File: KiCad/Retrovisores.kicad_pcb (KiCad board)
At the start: 2 copper layers, 63 parts, among them J1 Conn_01x02_Pin, J2 DE9_Pins, J4 DE9_Pins, J5 Conn_01x02_Pin, J6 Conn_01x02_Pin, J7 Conn_01x02_Pin, J8 Conn_PIC_ICSP_ICD, Q14 AO3400A, Q15 AO3401A, Q16 AO3400A, Q17 AO3401A, Q18 AO3400A, Q19 AO3401A, Q20 AO3400A, Q21 AO3401A, Q22 AO3400A, Q23 AO3401A, Q24 AO3400A, Q25 AO3401A, Q27 AO3400A, SW1 SW_Push, SW2 SW_Push, SW3 SW_Push, SW4 SW_Push, SW6 SW_Nidec_CAS-120A1, U1 SHTC3, U2 SN65HVD232, U4 LT1117-3.3, U5 TSR3-2450N, U6 VL53L1CXV0FY1, U7 PIC32MX250F128D-IPT, Y1 Crystal

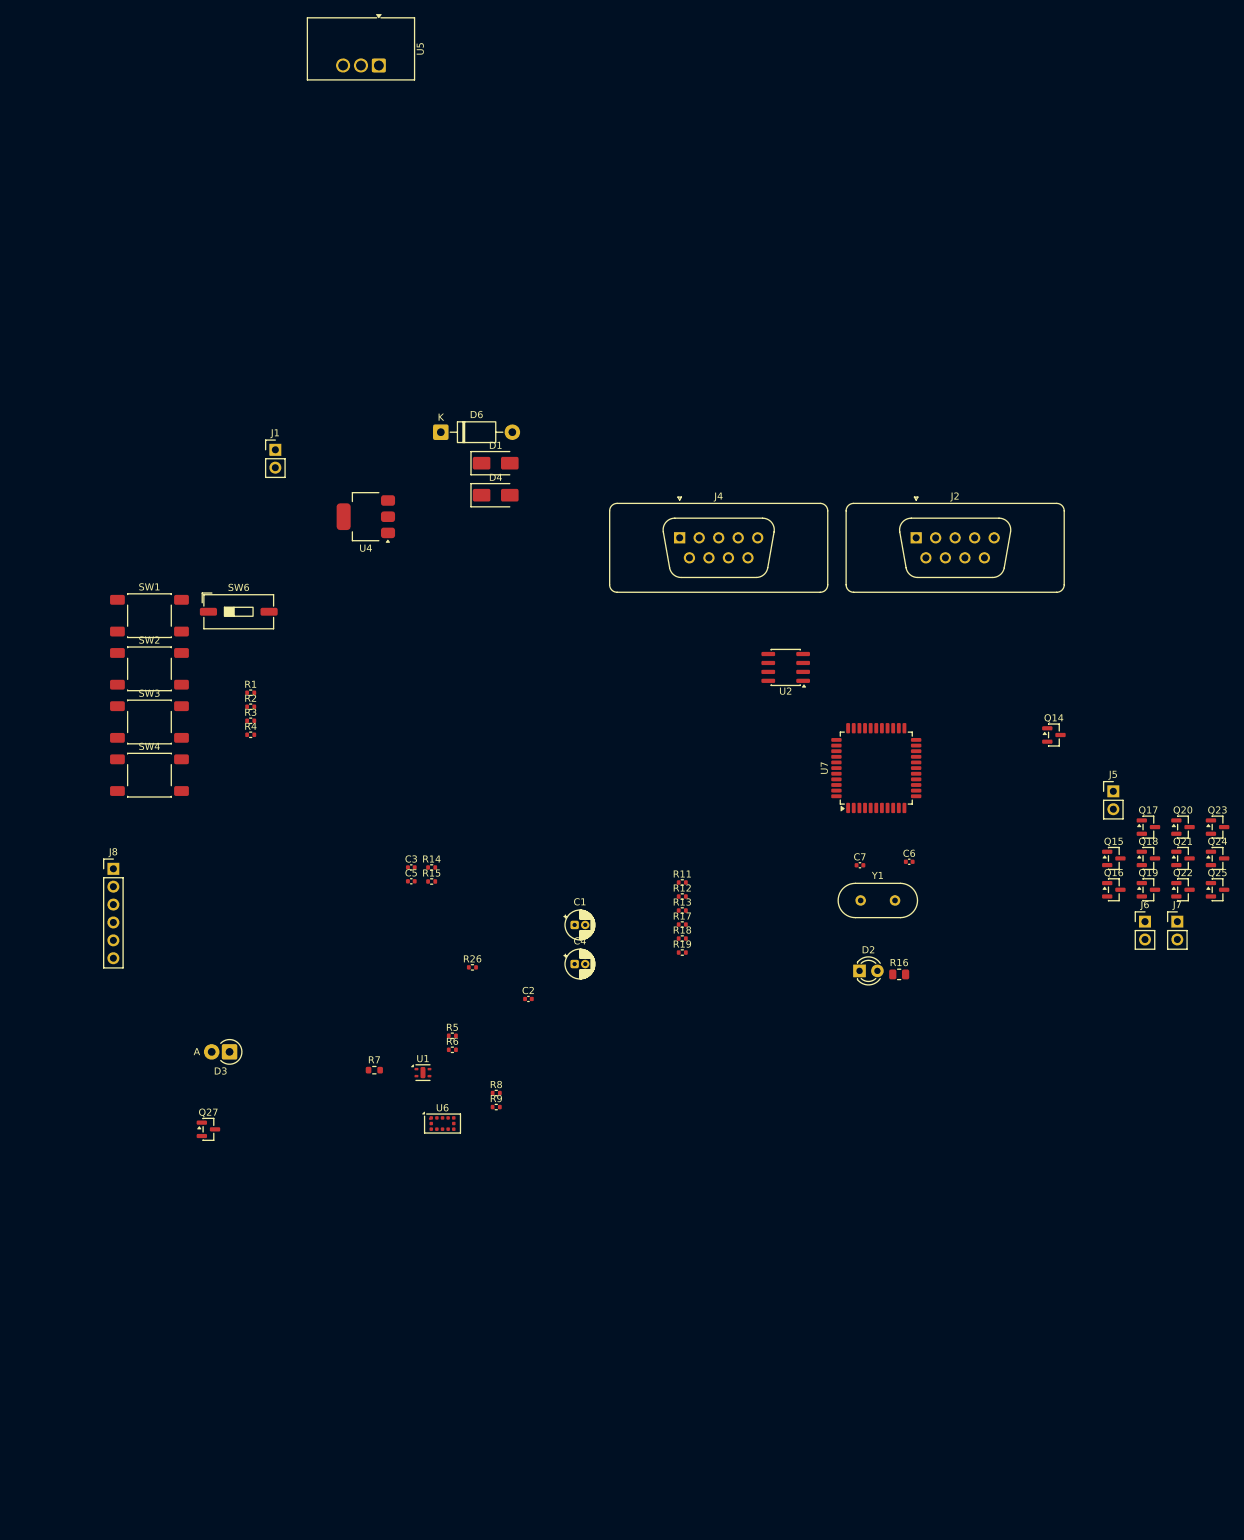
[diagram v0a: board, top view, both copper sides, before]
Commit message: he hecho el layout general menos el calefactor
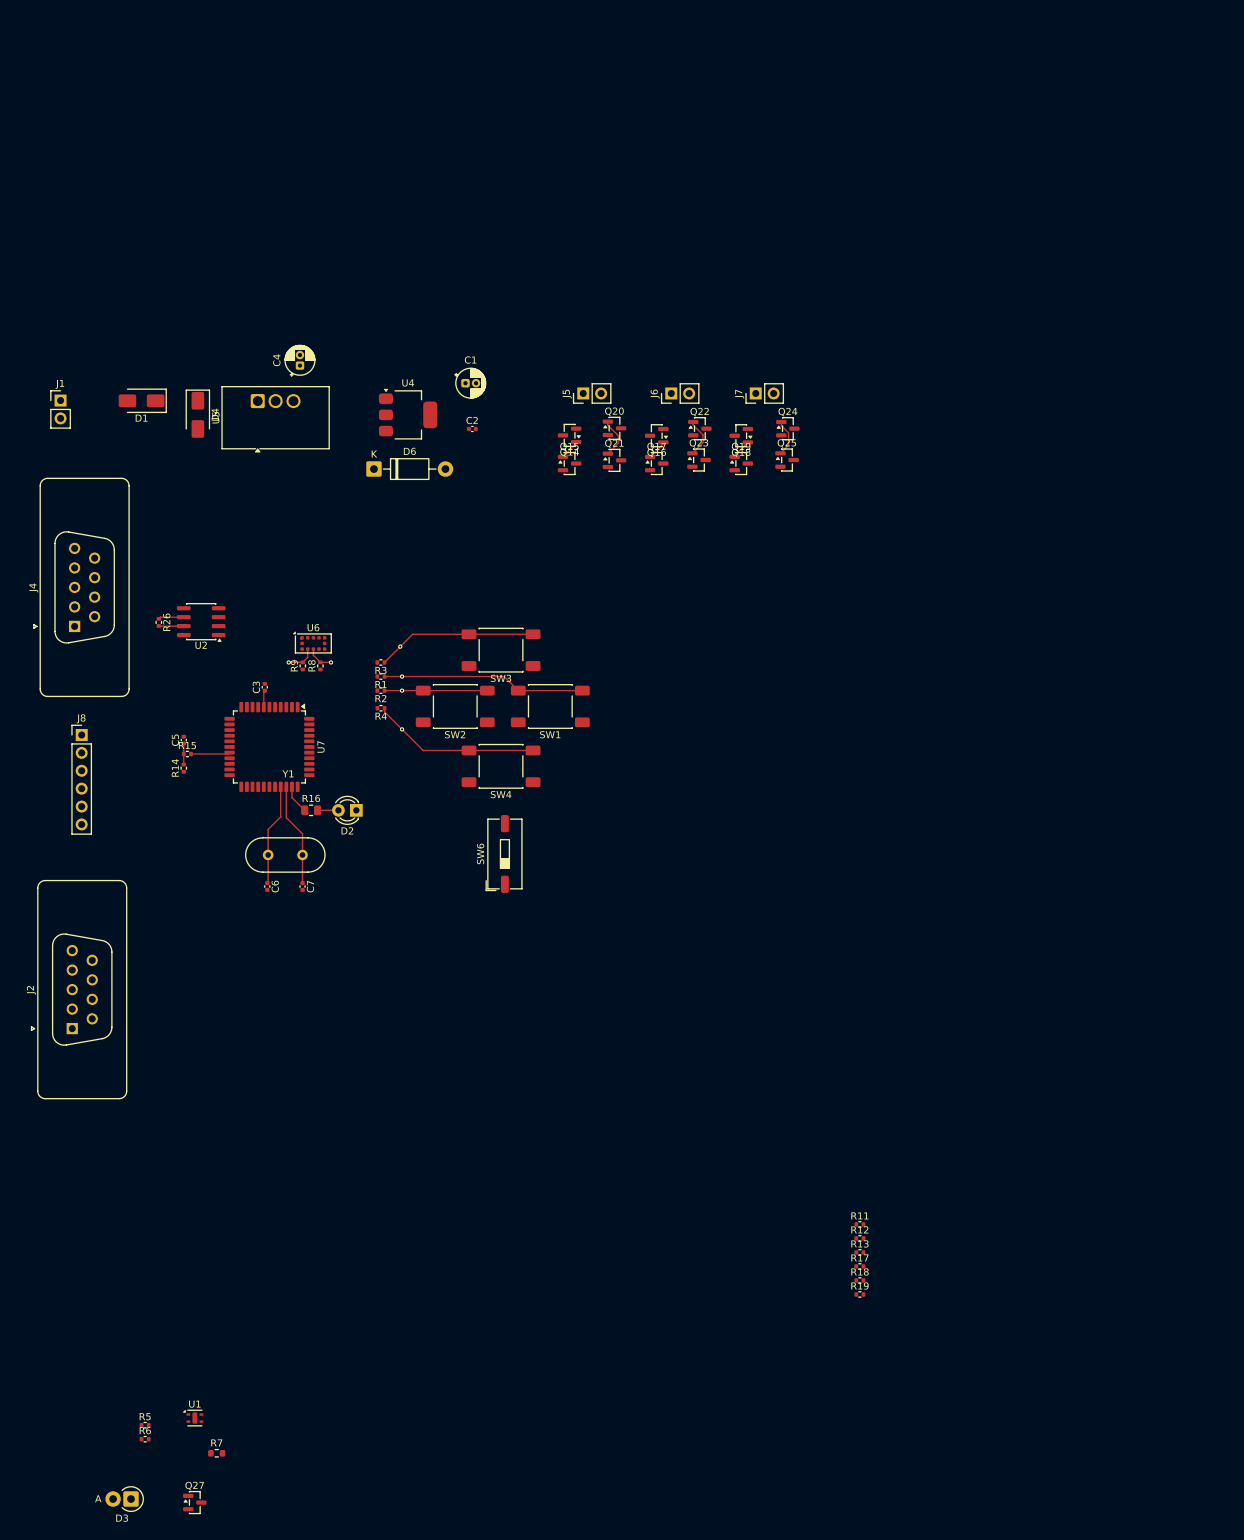
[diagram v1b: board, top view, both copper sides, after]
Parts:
- moved J2 138.6 mm to (93.2, 113.2), turned to 90 degrees
- moved J6 100.8 mm to (178.2, 23.0), turned to 90 degrees
- moved Q20 98.6 mm to (170.2, 27.9)
- moved Q21 98.6 mm to (170.2, 32.5)
- moved J7 96.0 mm to (190.2, 23.0), turned to 90 degrees
- moved Q15 95.5 mm to (163.8, 33.0)
- moved Q22 94.8 mm to (182.3, 28.0)
- moved J5 94.1 mm to (165.7, 23.0), turned to 90 degrees
- moved C4 93.5 mm to (125.5, 19.0), turned to 90 degrees
- moved Q16 91.5 mm to (176.2, 29.0), turned to 180 degrees
- moved C6 91.2 mm to (120.9, 93.0), turned to -90 degrees
- moved Q23 90.2 mm to (182.2, 32.5)
- moved J4 86.8 mm to (93.5, 56.1), turned to 90 degrees
- moved Q17 86.8 mm to (176.2, 33.0)
- moved R16 86.7 mm to (127.1, 82.2)
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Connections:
- U2 pad 1: R -> RCAN
- U2 pad 4: D -> DCAN
- U7 pad 33: R -> RCAN
- U7 pad 41: D -> DCAN
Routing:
- net R: track 0.00 -> 29.6 mm, vias 0 -> 1
- net D: track 0.00 -> 23.9 mm, vias 0 -> 1
- net U: track 0.00 -> 23.1 mm, vias 0 -> 1
- net OSC2: track 0.00 -> 14.6 mm
- net L: track 0.00 -> 14.6 mm, vias 0 -> 1
- net OSC1: track 0.00 -> 14.5 mm
- net SDL1: track 0.00 -> 5.79 mm
- net SDD1: track 0.00 -> 5.64 mm
- net MCLR: track 0.00 -> 5.56 mm
- net CL: track 0.00 -> 5.36 mm
- net KLKI2C: track 0.00 -> 4.18 mm, vias 0 -> 1
- net Net-(U7-RA8): track 0.00 -> 4.09 mm
- net DI2C: track 0.00 -> 3.80 mm, vias 0 -> 1
- net Net-(U2-CANL): track 0.00 -> 3.65 mm
- net Net-(U2-CANH): track 0.00 -> 3.56 mm
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
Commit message: añadido calefactor a la pcb
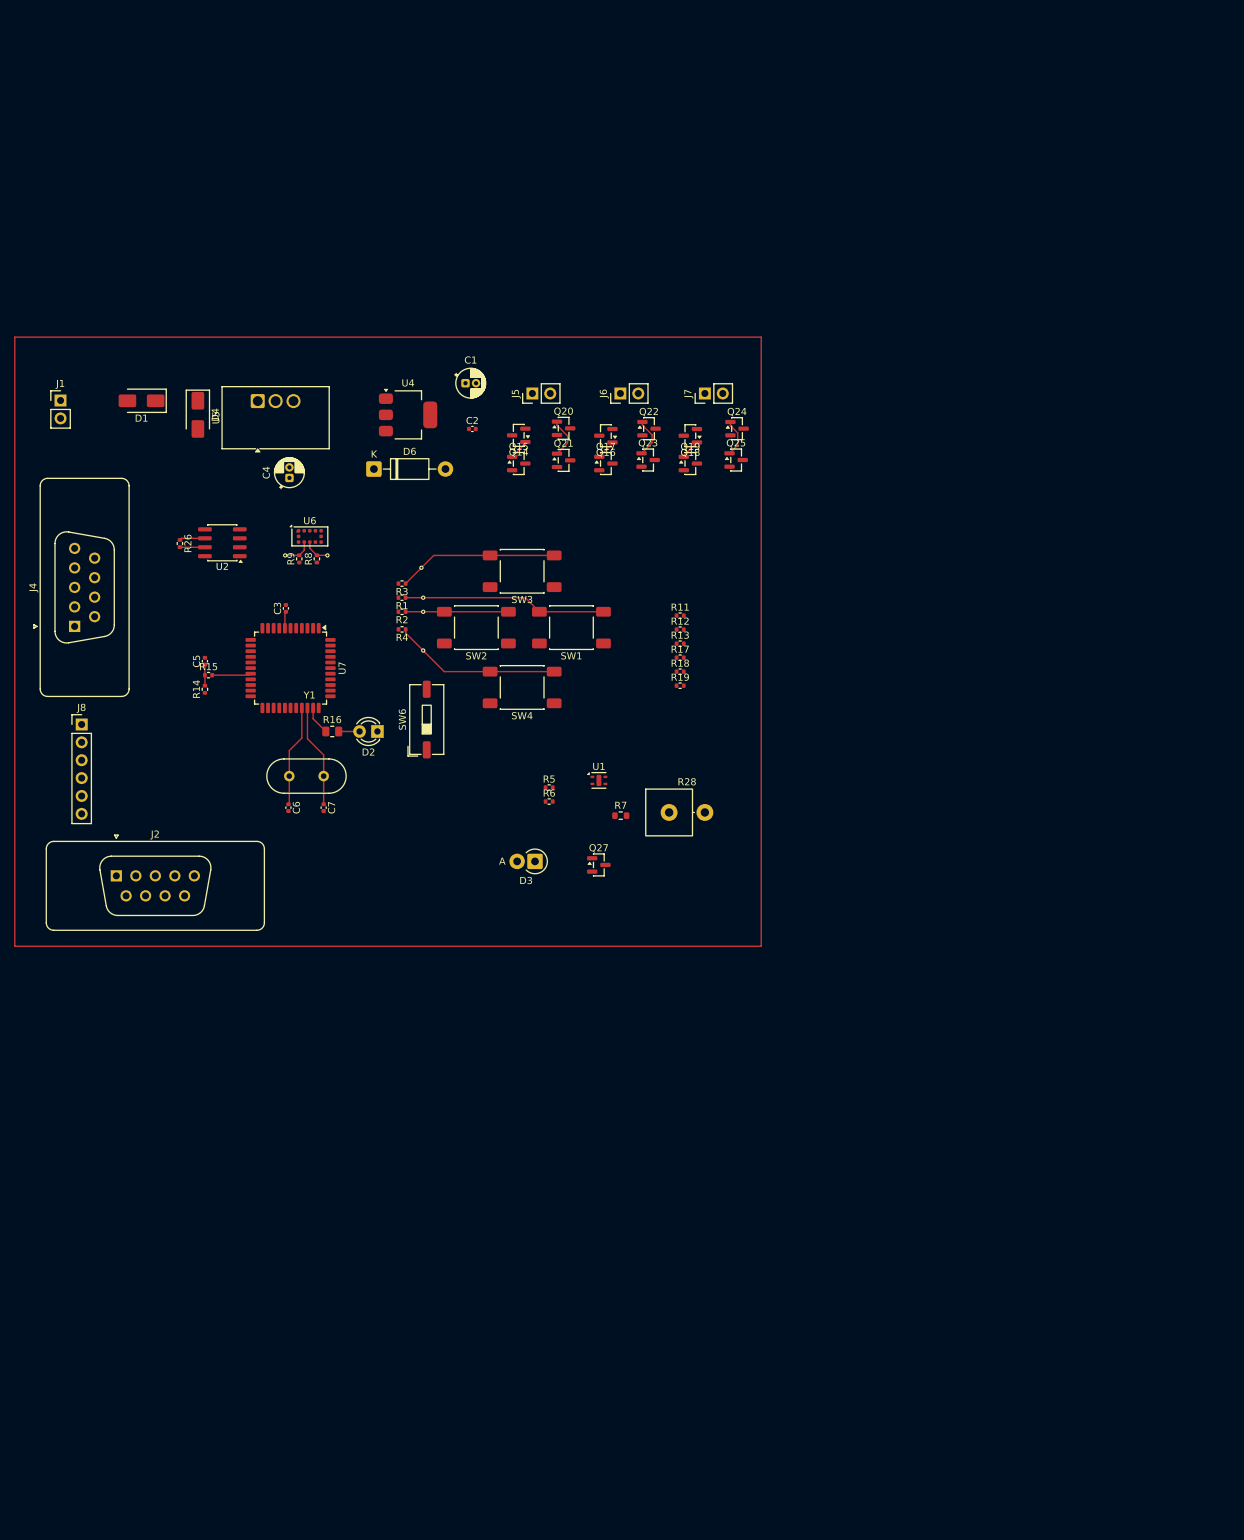
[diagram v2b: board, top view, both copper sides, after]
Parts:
- added R28: Heater, Resistor_THT:R_Axial_Power_L20.0mm_W6.4mm_P5.08mm_Vertical, F.Cu at (177.9, 82.5)
- moved R7 107.2 mm to (171.1, 83.0)
- moved D3 107.2 mm to (158.9, 89.5)
- moved Q27 107.2 mm to (167.9, 90.0)
- moved R5 107.2 mm to (160.9, 79.0)
- moved R6 107.2 mm to (160.9, 81.0)
- moved U1 107.2 mm to (167.9, 78.0)
- moved R12 90.1 mm to (179.5, 56.5)
- moved R18 90.1 mm to (179.5, 62.5)
- moved R11 90.1 mm to (179.5, 54.5)
- moved R13 90.1 mm to (179.5, 58.5)
- moved R17 90.1 mm to (179.5, 60.5)
- moved R19 90.1 mm to (179.5, 64.5)
- moved J2 22.6 mm to (99.4, 91.5), turned to 0 degrees
- moved SW6 22.1 mm to (143.5, 69.3)
- moved C4 16.0 mm to (124.0, 35.0)
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
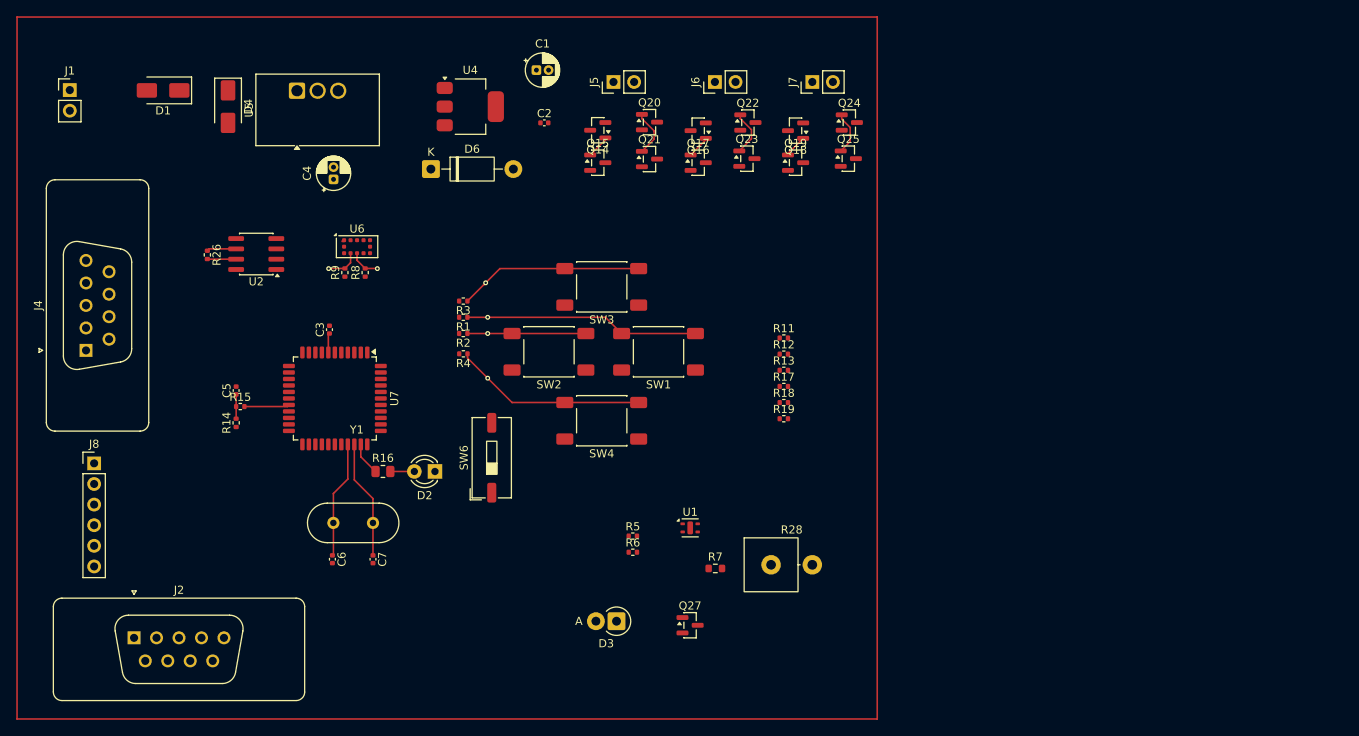
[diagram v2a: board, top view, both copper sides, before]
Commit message: cambiado placement a mejor
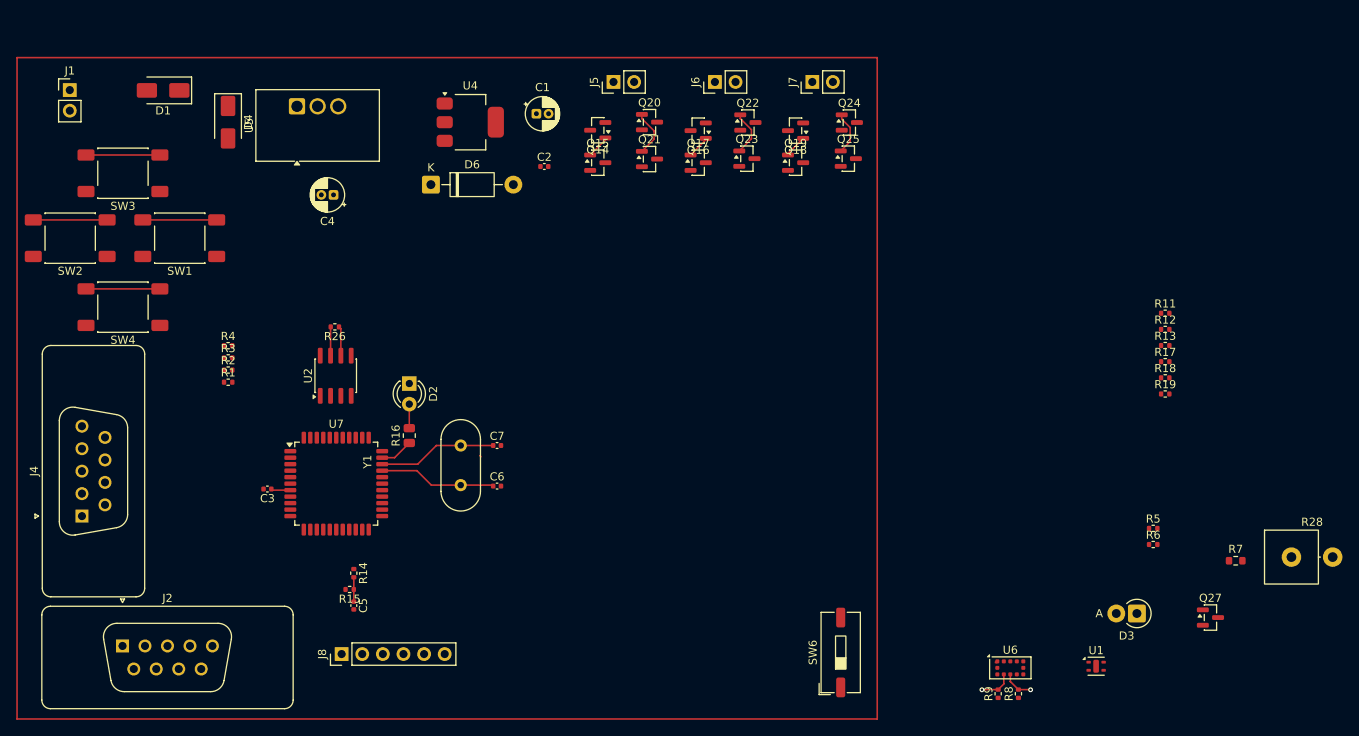
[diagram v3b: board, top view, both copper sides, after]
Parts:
- moved R8 95.8 mm to (208.4, 98.4)
- moved R9 95.8 mm to (205.9, 98.4)
- moved U6 95.8 mm to (207.4, 95.2)
- moved D3 64.1 mm to (223.0, 88.5)
- moved Q27 64.1 mm to (232.1, 89.0)
- moved R28 64.1 mm to (242.0, 81.5)
- moved R5 64.1 mm to (225.0, 78.0)
- moved R6 64.1 mm to (225.0, 80.0)
- moved R7 64.1 mm to (235.2, 82.0)
- moved SW1 60.6 mm to (105.0, 42.2)
- moved SW2 60.6 mm to (91.5, 42.2)
- moved SW3 60.6 mm to (98.0, 34.2)
- moved SW4 60.6 mm to (98.0, 50.8)
- moved U1 52.9 mm to (218.0, 95.0)
- moved SW6 49.2 mm to (186.5, 93.3)
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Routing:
- net R: track 29.6 -> 9.78 mm, vias 1 -> 0
- net D: track 23.9 -> 9.10 mm, vias 1 -> 0
- net U: track 23.1 -> 9.10 mm, vias 1 -> 0
- net L: track 14.6 -> 9.10 mm, vias 1 -> 0
- net MCLR: track 5.56 -> 0.28 mm
